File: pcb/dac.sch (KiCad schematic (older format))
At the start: 70 parts, among them U7 MAX5853ETL-T, U8 TLV3542IDR

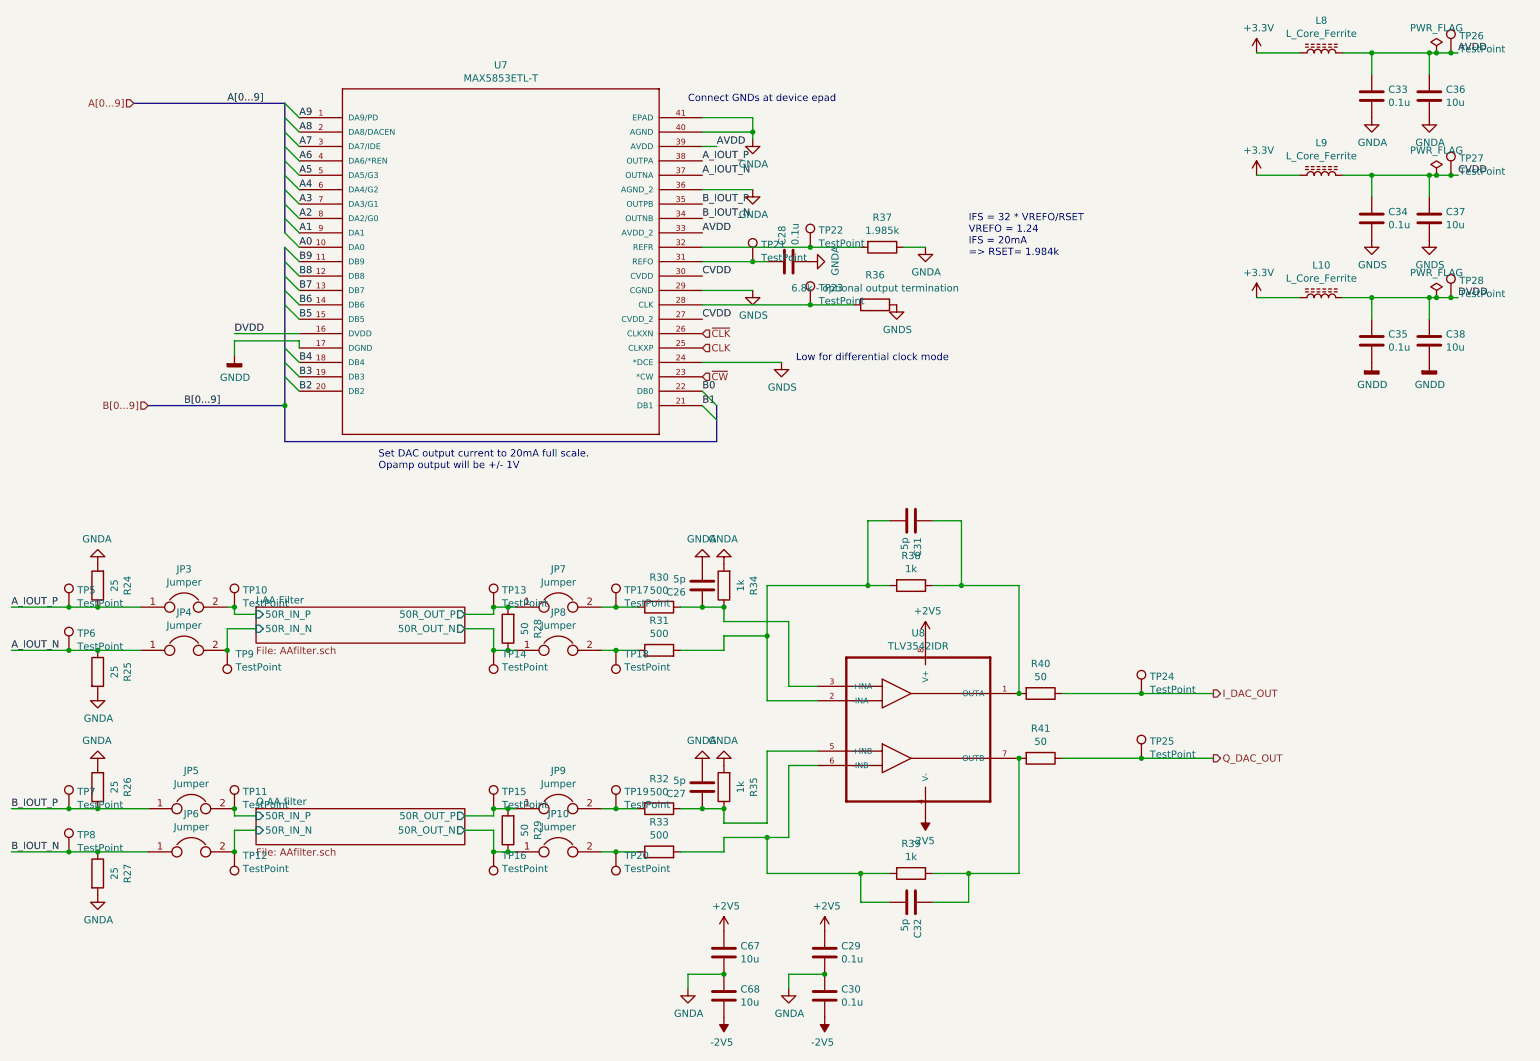
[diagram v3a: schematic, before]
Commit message: Update footprints, move to 0603 passives for JLCPCB assembly, create transformer footprints
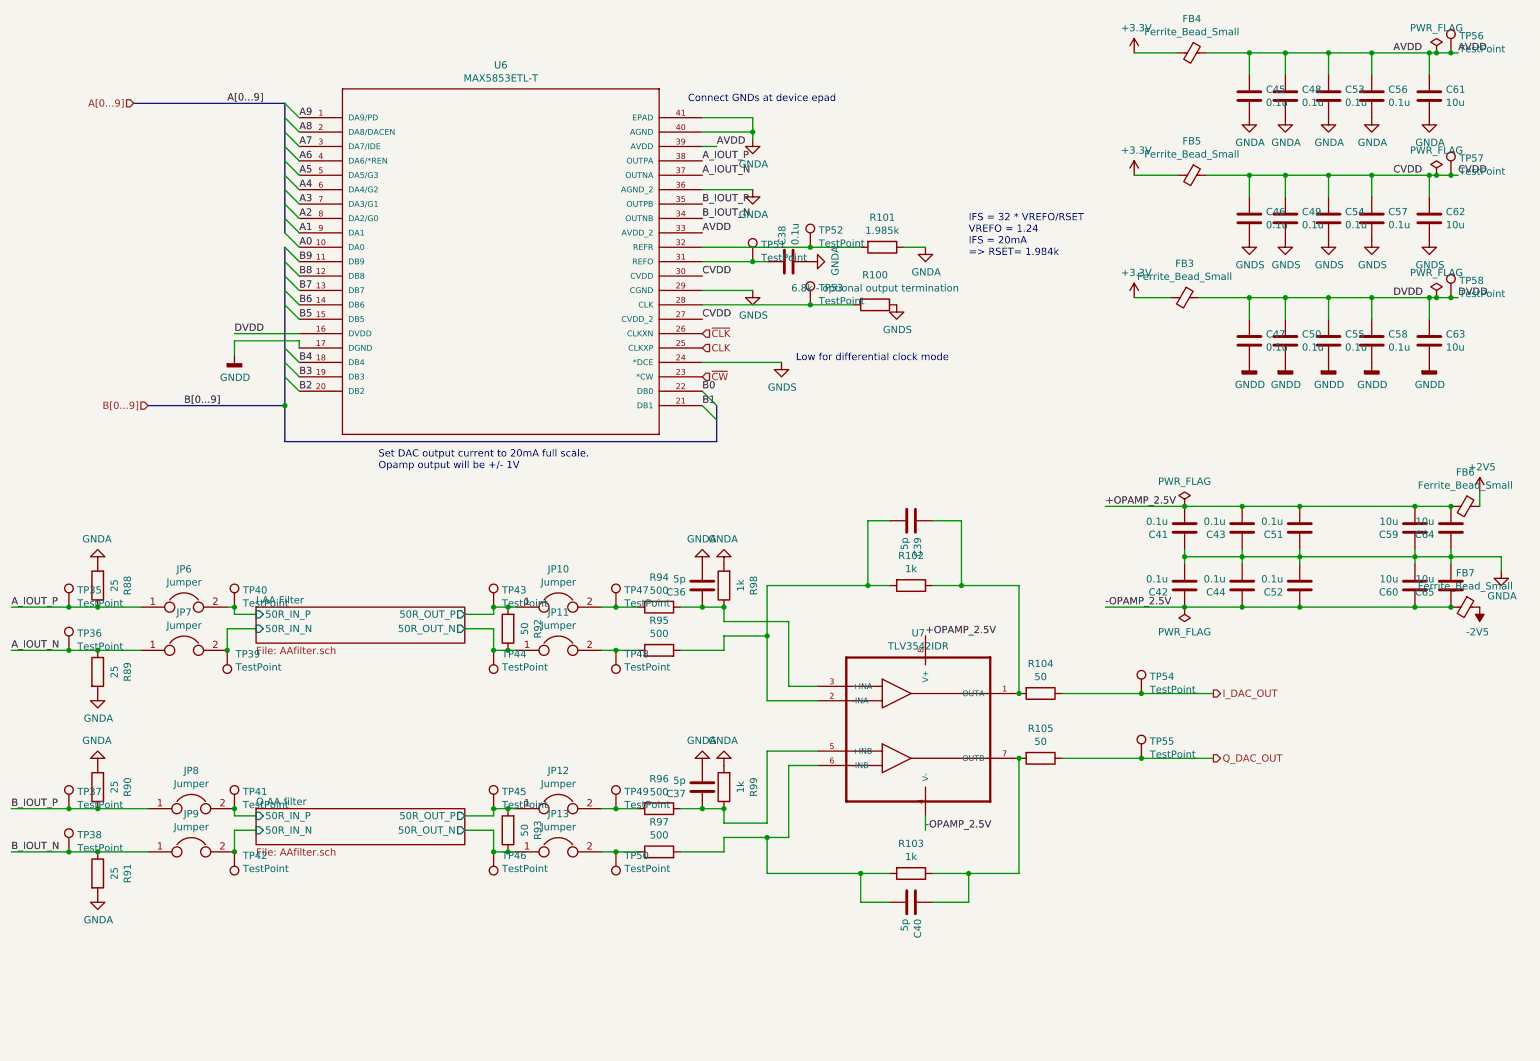
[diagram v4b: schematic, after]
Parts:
- removed C29, C30: 0.1u, Capacitor_SMD:C_0805_2012Metric_Pad1.15x1.40mm_HandSolder, symbol Device:C
- removed C67, C68: 10u, Capacitor_SMD:C_0805_2012Metric_Pad1.15x1.40mm_HandSolder, symbol Device:C
- removed L10, L8, L9: L_Core_Ferrite, symbol Device:L_Core_Ferrite
- added C41, C42, C43, C44, C45, C46, C47, C48, C49, C50, C51, C52, C53, C54, C55: 0.1u, Capacitor_SMD:C_0603_1608Metric, symbol Device:C
- added C59, C60, C64, C65: 10u, Capacitor_SMD:C_0603_1608Metric, symbol Device:C
- added FB3, FB4, FB5, FB6, FB7: Ferrite_Bead_Small, Inductor_SMD:L_0603_1608Metric_Pad1.05x0.95mm_HandSolder, symbol Device:Ferrite_Bead_Small
- C36: renamed from C26; footprint Capacitor_SMD:C_0805_2012Metric_Pad1.15x1.40mm_HandSolder -> Capacitor_SMD:C_0603_1608Metric
- C37: renamed from C27; footprint Capacitor_SMD:C_0805_2012Metric_Pad1.15x1.40mm_HandSolder -> Capacitor_SMD:C_0603_1608Metric
- C38: renamed from C28; footprint Capacitor_SMD:C_0805_2012Metric_Pad1.15x1.40mm_HandSolder -> Capacitor_SMD:C_0603_1608Metric
- C39: renamed from C31; footprint Capacitor_SMD:C_0805_2012Metric_Pad1.15x1.40mm_HandSolder -> Capacitor_SMD:C_0603_1608Metric
- C40: renamed from C32; footprint Capacitor_SMD:C_0805_2012Metric_Pad1.15x1.40mm_HandSolder -> Capacitor_SMD:C_0603_1608Metric
- C56: renamed from C33; footprint Capacitor_SMD:C_0805_2012Metric_Pad1.15x1.40mm_HandSolder -> Capacitor_SMD:C_0603_1608Metric
- C57: renamed from C34; footprint Capacitor_SMD:C_0805_2012Metric_Pad1.15x1.40mm_HandSolder -> Capacitor_SMD:C_0603_1608Metric
- C58: renamed from C35; footprint Capacitor_SMD:C_0805_2012Metric_Pad1.15x1.40mm_HandSolder -> Capacitor_SMD:C_0603_1608Metric
- C61: renamed from C36; footprint Capacitor_SMD:C_0805_2012Metric_Pad1.15x1.40mm_HandSolder -> Capacitor_SMD:C_0603_1608Metric
- C62: renamed from C37; footprint Capacitor_SMD:C_0805_2012Metric_Pad1.15x1.40mm_HandSolder -> Capacitor_SMD:C_0603_1608Metric
- C63: renamed from C38; footprint Capacitor_SMD:C_0805_2012Metric_Pad1.15x1.40mm_HandSolder -> Capacitor_SMD:C_0603_1608Metric
- R100: renamed from R36; footprint Resistor_SMD:R_0805_2012Metric_Pad1.20x1.40mm_HandSolder -> Resistor_SMD:R_0603_1608Metric
- R101: renamed from R37; footprint Resistor_SMD:R_0805_2012Metric_Pad1.20x1.40mm_HandSolder -> Resistor_SMD:R_0603_1608Metric
- R102: renamed from R38; footprint Resistor_SMD:R_0805_2012Metric_Pad1.20x1.40mm_HandSolder -> Resistor_SMD:R_0603_1608Metric
- R103: renamed from R39; footprint Resistor_SMD:R_0805_2012Metric_Pad1.20x1.40mm_HandSolder -> Resistor_SMD:R_0603_1608Metric
- R104: renamed from R40; footprint Resistor_SMD:R_0805_2012Metric_Pad1.20x1.40mm_HandSolder -> Resistor_SMD:R_0603_1608Metric
- R105: renamed from R41; footprint Resistor_SMD:R_0805_2012Metric_Pad1.20x1.40mm_HandSolder -> Resistor_SMD:R_0603_1608Metric
- R88: renamed from R24; footprint Resistor_SMD:R_0805_2012Metric_Pad1.20x1.40mm_HandSolder -> Resistor_SMD:R_0603_1608Metric
- R89: renamed from R25; footprint Resistor_SMD:R_0805_2012Metric_Pad1.20x1.40mm_HandSolder -> Resistor_SMD:R_0603_1608Metric
- R90: renamed from R26; footprint Resistor_SMD:R_0805_2012Metric_Pad1.20x1.40mm_HandSolder -> Resistor_SMD:R_0603_1608Metric
- R91: renamed from R27; footprint Resistor_SMD:R_0805_2012Metric_Pad1.20x1.40mm_HandSolder -> Resistor_SMD:R_0603_1608Metric
- R92: renamed from R28; footprint Resistor_SMD:R_0805_2012Metric_Pad1.20x1.40mm_HandSolder -> Resistor_SMD:R_0603_1608Metric
- R93: renamed from R29; footprint Resistor_SMD:R_0805_2012Metric_Pad1.20x1.40mm_HandSolder -> Resistor_SMD:R_0603_1608Metric
- R94: renamed from R30; footprint Resistor_SMD:R_0805_2012Metric_Pad1.20x1.40mm_HandSolder -> Resistor_SMD:R_0603_1608Metric
- R95: renamed from R31; footprint Resistor_SMD:R_0805_2012Metric_Pad1.20x1.40mm_HandSolder -> Resistor_SMD:R_0603_1608Metric
- R96: renamed from R32; footprint Resistor_SMD:R_0805_2012Metric_Pad1.20x1.40mm_HandSolder -> Resistor_SMD:R_0603_1608Metric
- R97: renamed from R33; footprint Resistor_SMD:R_0805_2012Metric_Pad1.20x1.40mm_HandSolder -> Resistor_SMD:R_0603_1608Metric
- R98: renamed from R34; footprint Resistor_SMD:R_0805_2012Metric_Pad1.20x1.40mm_HandSolder -> Resistor_SMD:R_0603_1608Metric
- R99: renamed from R35; footprint Resistor_SMD:R_0805_2012Metric_Pad1.20x1.40mm_HandSolder -> Resistor_SMD:R_0603_1608Metric
- TP35: renamed from TP5; footprint (none) -> TestPoint:TestPoint_Pad_D1.5mm
- TP36: renamed from TP6; footprint (none) -> TestPoint:TestPoint_Pad_D1.5mm
- TP37: renamed from TP7; footprint (none) -> TestPoint:TestPoint_Pad_D1.5mm
- TP38: renamed from TP8; footprint (none) -> TestPoint:TestPoint_Pad_D1.5mm
- TP39: renamed from TP9; footprint (none) -> TestPoint:TestPoint_Pad_D1.5mm
- TP40: renamed from TP10; footprint (none) -> TestPoint:TestPoint_Pad_D1.5mm
- TP41: renamed from TP11; footprint (none) -> TestPoint:TestPoint_Pad_D1.5mm
- TP42: renamed from TP12; footprint (none) -> TestPoint:TestPoint_Pad_D1.5mm
- TP43: renamed from TP13; footprint (none) -> TestPoint:TestPoint_Pad_D1.5mm
- TP44: renamed from TP14; footprint (none) -> TestPoint:TestPoint_Pad_D1.5mm
- TP45: renamed from TP15; footprint (none) -> TestPoint:TestPoint_Pad_D1.5mm
- TP46: renamed from TP16; footprint (none) -> TestPoint:TestPoint_Pad_D1.5mm
- TP47: renamed from TP17; footprint (none) -> TestPoint:TestPoint_Pad_D1.5mm
- TP48: renamed from TP18; footprint (none) -> TestPoint:TestPoint_Pad_D1.5mm
- TP49: renamed from TP19; footprint (none) -> TestPoint:TestPoint_Pad_D1.5mm
- TP50: renamed from TP20; footprint (none) -> TestPoint:TestPoint_Pad_D1.5mm
- TP51: renamed from TP21; footprint (none) -> TestPoint:TestPoint_Pad_D1.5mm
- TP52: renamed from TP22; footprint (none) -> TestPoint:TestPoint_Pad_D1.5mm
- TP53: renamed from TP23; footprint (none) -> TestPoint:TestPoint_Pad_D1.5mm
- TP54: renamed from TP24; footprint (none) -> TestPoint:TestPoint_Pad_D1.5mm
- TP55: renamed from TP25; footprint (none) -> TestPoint:TestPoint_Pad_D1.5mm
- TP56: renamed from TP26; footprint (none) -> TestPoint:TestPoint_Pad_D1.5mm
- TP57: renamed from TP27; footprint (none) -> TestPoint:TestPoint_Pad_D1.5mm
- TP58: renamed from TP28; footprint (none) -> TestPoint:TestPoint_Pad_D1.5mm
- U6: renamed from U7; footprint (none) -> Package_DFN_QFN:QFN-40-1EP_6x6mm_P0.5mm_EP4.6x4.6mm_ThermalVias
- U7: renamed from U8; footprint (none) -> Package_SO:SOIC-8_3.9x4.9mm_P1.27mm
- renumbered JP7 to JP10, JP8 to JP11, JP9 to JP12, JP10 to JP13, JP3 to JP6, JP4 to JP7, JP5 to JP8, JP6 to JP9
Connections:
- net +2V5: now also FB6.1; no longer U7.8 (V+)
- net +3V3: now also FB3.2, FB4.2, FB5.2
- net -2V5: now also FB7.1; no longer U7.4 (V-)
- net AVDD: now also C45.1, C48.1, C53.1, FB4.1
- net CVDD: now also C46.1, C49.1, C54.1, FB5.1
- net DVDD: now also C47.1, C50.1, C55.1, FB3.1
- net GNDA: now also C41.1, C42.2, C43.1, C44.2, C45.2, C48.2, C51.1, C52.2, C53.2, C59.1, C60.2, C64.1, C65.2
- net GNDD: now also C47.2, C50.2, C55.2
- net GNDS: now also C46.2, C49.2, C54.2
- new net +OPAMP_2.5V: C41.2, C43.2, C51.2, C59.2, C64.2, FB6.2, U7.8 (V+)
- new net -OPAMP_2.5V: C42.1, C44.1, C52.1, C60.1, C65.1, FB7.2, U7.4 (V-)

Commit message: finish up vregs, routed filters, iq baseband outputs
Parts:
- FB3, FB4, FB5, FB6, FB7: footprint Inductor_SMD:L_0603_1608Metric_Pad1.05x0.95mm_HandSolder -> Inductor_SMD:L_0805_2012Metric_Pad1.05x1.20mm_HandSolder
- JP10, JP11, JP12, JP13, JP6, JP7, JP8, JP9: footprint (none) -> Resistor_SMD:R_0603_1608Metric
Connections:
- net I_FB_N: now reaches C39.2, R102.2, R95.2, U7.2 (-INA)
- net I_FB_P: now reaches C36.1, R94.1, R98.1, U7.3 (+INA)
- net Q_FB_P: now reaches C37.1, R96.1, R99.1, U7.5 (+INB)
- net Q_FB_N: now reaches C40.2, R103.2, R97.2, U7.6 (-INB)
- net I_F_N: now reaches JP11.2, R95.1, TP48.1
- net I_F_P: now reaches JP10.2, R94.2, TP47.1
- net Q_F_N: now reaches JP13.2, R97.1, TP50.1
- net Q_F_P: now reaches JP12.2, R96.2, TP49.1
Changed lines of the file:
@@
 F 0 "JP6" H 1750 5014 50  0000 C CNN
 F 1 "Jumper" H 1750 4923 50  0000 C CNN
-F 2 "" H 1750 4750 50  0001 C CNN
+F 2 "Resistor_SMD:R_0603_1608Metric" H 1750 4750 50  0001 C CNN
 F 3 "~" H 1750 4750 50  0001 C CNN
 	1    1750 4750
@@
 F 0 "JP7" H 1750 5314 50  0000 C CNN
 F 1 "Jumper" H 1750 5223 50  0000 C CNN
-F 2 "" H 1750 5050 50  0001 C CNN
+F 2 "Resistor_SMD:R_0603_1608Metric" H 1750 5050 50  0001 C CNN
 F 3 "~" H 1750 5050 50  0001 C CNN
 	1    1750 5050
@@
 F 0 "JP8" H 1800 6414 50  0000 C CNN
 F 1 "Jumper" H 1800 6323 50  0000 C CNN
-F 2 "" H 1800 6150 50  0001 C CNN
+F 2 "Resistor_SMD:R_0603_1608Metric" H 1800 6150 50  0001 C CNN
 F 3 "~" H 1800 6150 50  0001 C CNN
 	1    1800 6150
@@
 F 0 "JP9" H 1800 6714 50  0000 C CNN
 F 1 "Jumper" H 1800 6623 50  0000 C CNN
-F 2 "" H 1800 6450 50  0001 C CNN
+F 2 "Resistor_SMD:R_0603_1608Metric" H 1800 6450 50  0001 C CNN
 F 3 "~" H 1800 6450 50  0001 C CNN
 	1    1800 6450
@@
 F 0 "JP10" H 4350 5014 50  0000 C CNN
 F 1 "Jumper" H 4350 4923 50  0000 C CNN
-F 2 "" H 4350 4750 50  0001 C CNN
+F 2 "Resistor_SMD:R_0603_1608Metric" H 4350 4750 50  0001 C CNN
 F 3 "~" H 4350 4750 50  0001 C CNN
 	1    4350 4750
@@
 F 0 "JP11" H 4350 5314 50  0000 C CNN
 F 1 "Jumper" H 4350 5223 50  0000 C CNN
-F 2 "" H 4350 5050 50  0001 C CNN
+F 2 "Resistor_SMD:R_0603_1608Metric" H 4350 5050 50  0001 C CNN
 F 3 "~" H 4350 5050 50  0001 C CNN
 	1    4350 5050
@@
 F 0 "JP12" H 4350 6414 50  0000 C CNN
 F 1 "Jumper" H 4350 6323 50  0000 C CNN
-F 2 "" H 4350 6150 50  0001 C CNN
+F 2 "Resistor_SMD:R_0603_1608Metric" H 4350 6150 50  0001 C CNN
 F 3 "~" H 4350 6150 50  0001 C CNN
 	1    4350 6150
@@
 F 0 "JP13" H 4350 6714 50  0000 C CNN
 F 1 "Jumper" H 4350 6623 50  0000 C CNN
-F 2 "" H 4350 6450 50  0001 C CNN
+F 2 "Resistor_SMD:R_0603_1608Metric" H 4350 6450 50  0001 C CNN
 F 3 "~" H 4350 6450 50  0001 C CNN
 	1    4350 6450
@@
 F 0 "FB4" V 8513 900 50  0000 C CNN
 F 1 "Ferrite_Bead_Small" V 8604 900 50  0000 C CNN
-F 2 "Inductor_SMD:L_0603_1608Metric_Pad1.05x0.95mm_HandSolder" V 8680 900 50  0001 C CNN
+F 2 "Inductor_SMD:L_0805_2012Metric_Pad1.05x1.20mm_HandSolder" V 8680 900 50  0001 C CNN
 F 3 "~" H 8750 900 50  0001 C CNN
 	1    8750 900
@@
 F 0 "FB5" V 8513 1750 50  0000 C CNN
 F 1 "Ferrite_Bead_Small" V 8604 1750 50  0000 C CNN
-F 2 "Inductor_SMD:L_0603_1608Metric_Pad1.05x0.95mm_HandSolder" V 8680 1750 50  0001 C CNN
+F 2 "Inductor_SMD:L_0805_2012Metric_Pad1.05x1.20mm_HandSolder" V 8680 1750 50  0001 C CNN
 F 3 "~" H 8750 1750 50  0001 C CNN
 	1    8750 1750
@@
 F 0 "FB3" V 8463 2600 50  0000 C CNN
 F 1 "Ferrite_Bead_Small" V 8554 2600 50  0000 C CNN
-F 2 "Inductor_SMD:L_0603_1608Metric_Pad1.05x0.95mm_HandSolder" V 8630 2600 50  0001 C CNN
+F 2 "Inductor_SMD:L_0805_2012Metric_Pad1.05x1.20mm_HandSolder" V 8630 2600 50  0001 C CNN
 F 3 "~" H 8700 2600 50  0001 C CNN
 	1    8700 2600
@@
 F 0 "FB6" V 10413 4050 50  0000 C CNN
 F 1 "Ferrite_Bead_Small" V 10504 4050 50  0000 C CNN
-F 2 "Inductor_SMD:L_0603_1608Metric_Pad1.05x0.95mm_HandSolder" V 10580 4050 50  0001 C CNN
+F 2 "Inductor_SMD:L_0805_2012Metric_Pad1.05x1.20mm_HandSolder" V 10580 4050 50  0001 C CNN
 F 3 "~" H 10650 4050 50  0001 C CNN
 	1    10650 4050
@@
 F 0 "FB7" V 10413 4750 50  0000 C CNN
 F 1 "Ferrite_Bead_Small" V 10504 4750 50  0000 C CNN
-F 2 "Inductor_SMD:L_0603_1608Metric_Pad1.05x0.95mm_HandSolder" V 10580 4750 50  0001 C CNN
+F 2 "Inductor_SMD:L_0805_2012Metric_Pad1.05x1.20mm_HandSolder" V 10580 4750 50  0001 C CNN
 F 3 "~" H 10650 4750 50  0001 C CNN
 	1    10650 4750
@@
 Wire Bus Line
 	2450 2250 2450 3350
+Text Label 4700 4750 0    50   ~ 0
+I_F_P
+Text Label 4700 5050 0    50   ~ 0
+I_F_N
+Text Label 4700 6150 0    50   ~ 0
+Q_F_P
+Text Label 4700 6450 0    50   ~ 0
+Q_F_N
+Text Label 5550 4850 0    50   ~ 0
+I_FB_P
+Text Label 5550 4950 0    50   ~ 0
+I_FB_N
+Text Label 5550 6250 0    50   ~ 0
+Q_FB_P
+Text Label 5550 6350 0    50   ~ 0
+Q_FB_N
 $EndSCHEMATC

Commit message: layout progress
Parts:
- removed C47, C50: 0.1u, Capacitor_SMD:C_0603_1608Metric, symbol Device:C
- removed TP54, TP55: TestPoint, TestPoint:TestPoint_Pad_D1.5mm, symbol Connector:TestPoint
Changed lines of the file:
@@
 F5 "50R_OUT_P" O R 3700 6200 50
 $EndSheet
-Wire Wire Line
-	7850 5350 8400 5350
-Wire Wire Line
-	7850 5800 8400 5800
 Text HLabel 8900 5350 2    50   Output ~ 0
 I_DAC_OUT
 Text HLabel 8900 5800 2    50   Output ~ 0
 Q_DAC_OUT
-$Comp
-L Connector:TestPoint TP54
-U 1 1 5FC2A50D
-P 8400 5350
-F 0 "TP54" H 8458 5468 50  0000 L CNN
-F 1 "TestPoint" H 8458 5377 50  0000 L CNN
-F 2 "TestPoint:TestPoint_Pad_D1.5mm" H 8600 5350 50  0001 C CNN
-F 3 "~" H 8600 5350 50  0001 C CNN
-	1    8400 5350
-	1    0    0    -1
-$EndComp
-Connection ~ 8400 5350
-Wire Wire Line
-	8400 5350 8900 5350
-$Comp
-L Connector:TestPoint TP55
-U 1 1 5FC2B18F
-P 8400 5800
-F 0 "TP55" H 8458 5918 50  0000 L CNN
-F 1 "TestPoint" H 8458 5827 50  0000 L CNN
-F 2 "TestPoint:TestPoint_Pad_D1.5mm" H 8600 5800 50  0001 C CNN
-F 3 "~" H 8600 5800 50  0001 C CNN
-	1    8400 5800
-	1    0    0    -1
-$EndComp
-Connection ~ 8400 5800
-Wire Wire Line
-	8400 5800 8900 5800
 $Comp
 L Connector:TestPoint TP35
@@
 $Comp
 L Device:C C?
-U 1 1 5FC7FF51
-P 9150 2900
-AR Path="/5FC7FF51" Ref="C?"  Part="1"
-AR Path="/5FB3742F/5FC7FF51" Ref="C47"  Part="1"
-F 0 "C47" H 9265 2946 50  0000 L CNN
-F 1 "0.1u" H 9265 2855 50  0000 L CNN
-F 2 "Capacitor_SMD:C_0603_1608Metric" H 9188 2750 50  0001 C CNN
-F 3 "~" H 9150 2900 50  0001 C CNN
-	1    9150 2900
-	1    0    0    -1
-$EndComp
-Wire Wire Line
-	9150 2750 9150 2600
-$Comp
-L Device:C C?
-U 1 1 5FC886FD
-P 9400 2900
-AR Path="/5FC886FD" Ref="C?"  Part="1"
-AR Path="/5FB3742F/5FC886FD" Ref="C50"  Part="1"
-F 0 "C50" H 9515 2946 50  0000 L CNN
-F 1 "0.1u" H 9515 2855 50  0000 L CNN
-F 2 "Capacitor_SMD:C_0603_1608Metric" H 9438 2750 50  0001 C CNN
-F 3 "~" H 9400 2900 50  0001 C CNN
-	1    9400 2900
-	1    0    0    -1
-$EndComp
-Wire Wire Line
-	9400 2750 9400 2600
-$Comp
-L Device:C C?
 U 1 1 5FC910BC
 P 9700 2900
@@
 	9700 2750 9700 2600
 Connection ~ 9700 2600
-Wire Wire Line
-	9700 2600 9400 2600
-Connection ~ 9400 2600
-Wire Wire Line
-	9400 2600 9150 2600
-Connection ~ 9150 2600
 Connection ~ 9150 1750
 Connection ~ 9400 1750
@@
 $EndComp
 $Comp
-L power:GNDD #PWR?
-U 1 1 5FCC9D7A
-P 9400 3050
-AR Path="/5FCC9D7A" Ref="#PWR?"  Part="1"
-AR Path="/5FB3742F/5FCC9D7A" Ref="#PWR095"  Part="1"
-F 0 "#PWR095" H 9400 2800 50  0001 C CNN
-F 1 "GNDD" H 9404 2895 50  0000 C CNN
-F 2 "" H 9400 3050 50  0001 C CNN
-F 3 "" H 9400 3050 50  0001 C CNN
-	1    9400 3050
-	1    0    0    -1
-$EndComp
-$Comp
-L power:GNDD #PWR?
-U 1 1 5FCCA15D
-P 9150 3050
-AR Path="/5FCCA15D" Ref="#PWR?"  Part="1"
-AR Path="/5FB3742F/5FCCA15D" Ref="#PWR092"  Part="1"
-F 0 "#PWR092" H 9150 2800 50  0001 C CNN
-F 1 "GNDD" H 9154 2895 50  0000 C CNN
-F 2 "" H 9150 3050 50  0001 C CNN
-F 3 "" H 9150 3050 50  0001 C CNN
-	1    9150 3050
-	1    0    0    -1
-$EndComp
-$Comp
 L power:GNDS #PWR?
 U 1 1 5FCCB637
@@
 	0    1    1    0
 $EndComp
-Wire Wire Line
-	8800 2600 9150 2600
 $Comp
 L Device:Ferrite_Bead_Small FB6
@@
 	-1   0    0    1
 $EndComp
-Wire Bus Line
-	5450 3350 5450 3600
-Wire Bus Line
-	2450 1250 2450 2150
-Wire Bus Line
-	2450 2250 2450 3350
 Text Label 4700 4750 0    50   ~ 0
 I_F_P
@@
 Text Label 5550 6350 0    50   ~ 0
 Q_FB_N
+Wire Wire Line
+	7850 5350 8900 5350
+Wire Wire Line
+	7850 5800 8900 5800
+Wire Wire Line
+	8800 2600 9700 2600
+Wire Bus Line
+	5450 3350 5450 3600
+Wire Bus Line
+	2450 1250 2450 2150
+Wire Bus Line
+	2450 2250 2450 3350
 $EndSCHEMATC
